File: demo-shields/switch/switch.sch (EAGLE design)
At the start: 18 parts, among them J4 J5MM, T1 2N2222

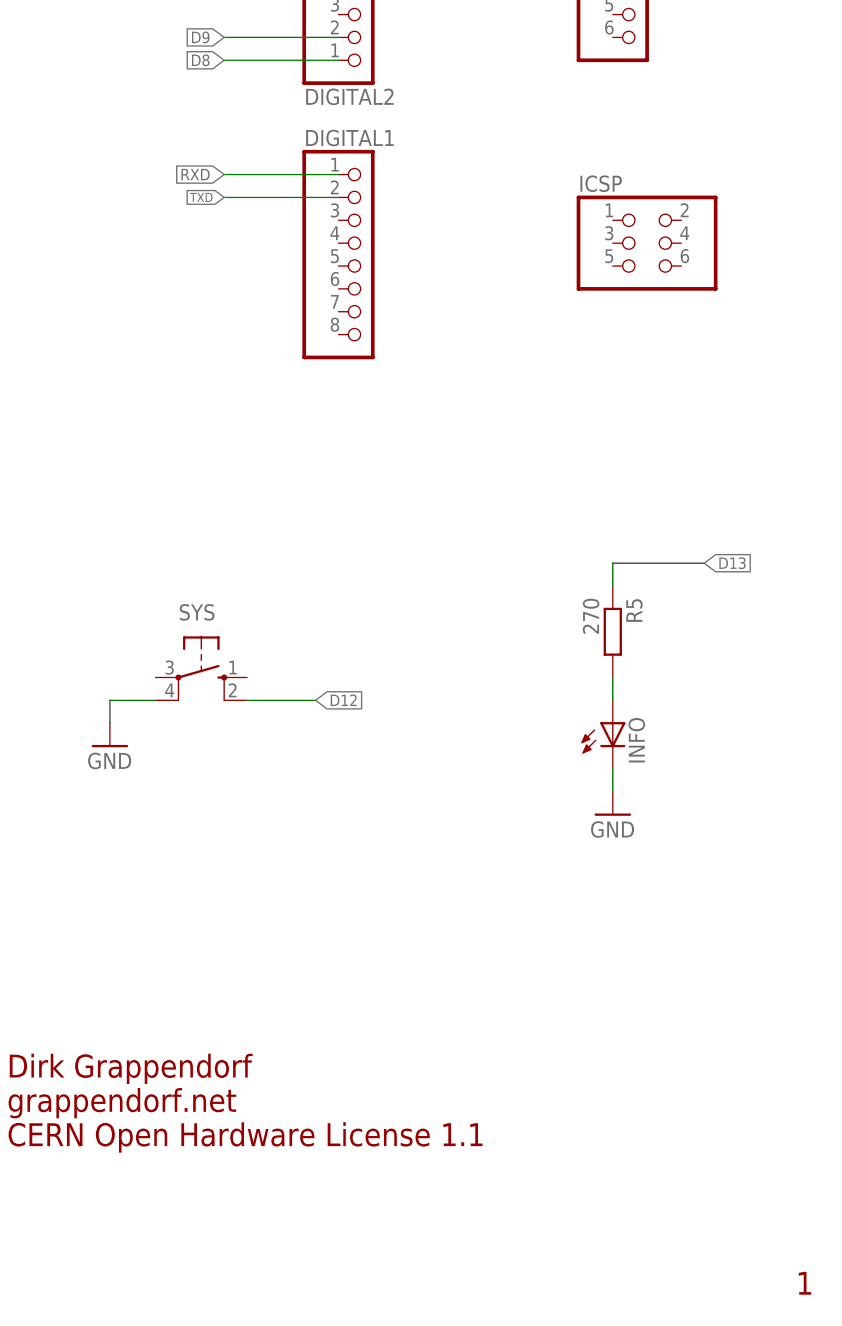
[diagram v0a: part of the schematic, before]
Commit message: fix: Use software serial for WiFly communication
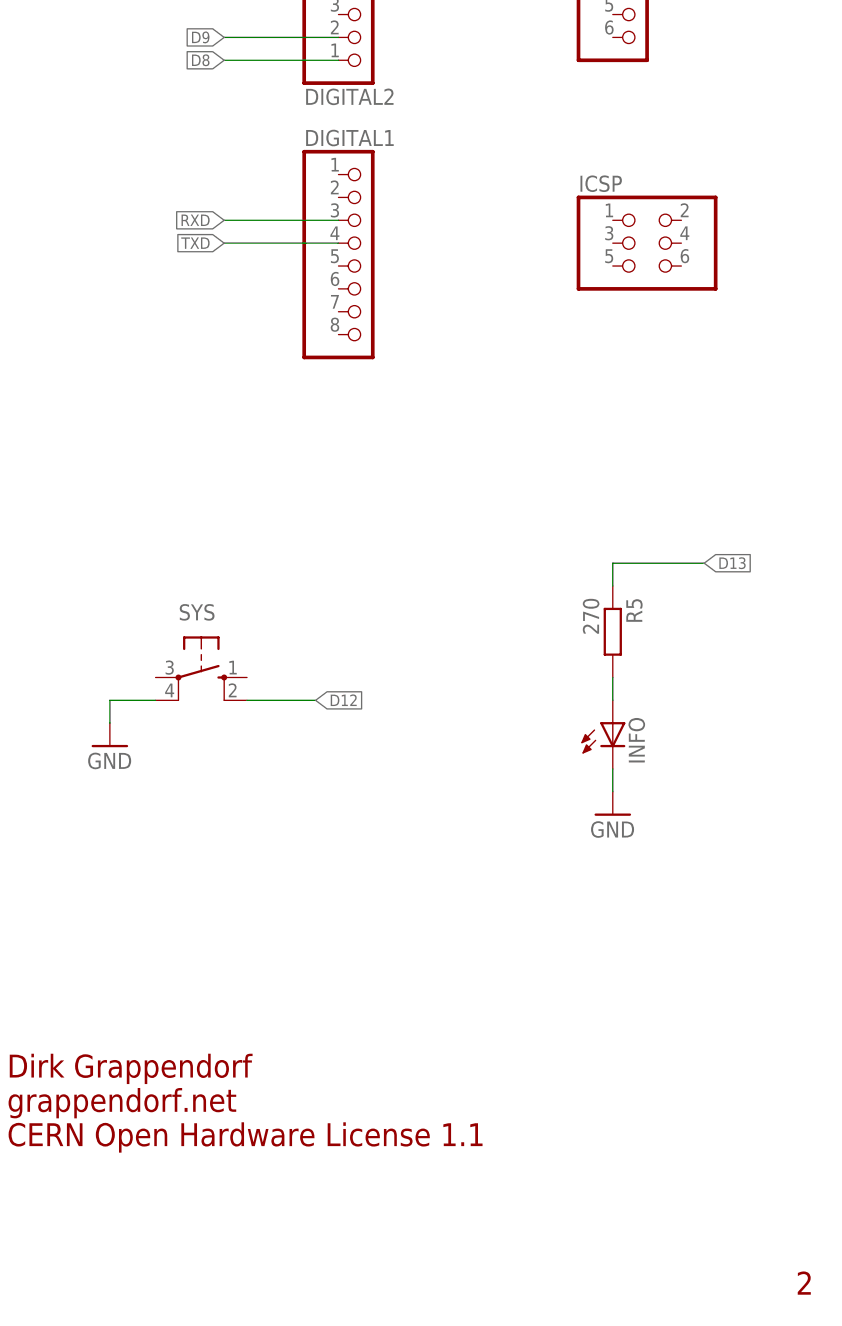
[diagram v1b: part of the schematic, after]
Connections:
- net RXD: now also DIGITAL1.3; no longer DIGITAL1.1
- net TXD: now also DIGITAL1.4; no longer DIGITAL1.2
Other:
- note added: "2"
- note removed: "1"
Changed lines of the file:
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@@
 <plain>
 <text x="163.83" y="31.75" size="2.54" layer="94">Dirk Grappendorf</text>
-<text x="251.46" y="7.62" size="2.54" layer="94">1</text>
+<text x="251.46" y="7.62" size="2.54" layer="94">2</text>
 <text x="163.83" y="27.94" size="2.54" layer="94">grappendorf.net</text>
 <text x="163.83" y="24.13" size="2.54" layer="94">CERN Open Hardware License 1.1</text>
@@
 <net name="RXD" class="0">
 <segment>
-<pinref part="DIGITAL1" gate="A" pin="1"/>
-<wire x1="200.66" y1="132.08" x2="187.96" y2="132.08" width="0.1524" layer="91"/>
-<label x="187.96" y="132.08" size="1.27" layer="95" rot="R180" xref="yes"/>
-</segment>
-<segment>
 <pinref part="WIFLY" gate="G$1" pin="DOUT"/>
 <wire x1="45.72" y1="149.86" x2="38.1" y2="149.86" width="0.1524" layer="91"/>
 <label x="38.1" y="149.86" size="1.27" layer="95" rot="R180" xref="yes"/>
+</segment>
+<segment>
+<pinref part="DIGITAL1" gate="A" pin="3"/>
+<wire x1="200.66" y1="127" x2="187.96" y2="127" width="0.1524" layer="91"/>
+<label x="187.96" y="127" size="1.27" layer="95" rot="R180" xref="yes"/>
 </segment>
 </net>
@@
 <net name="TXD" class="0">
 <segment>
-<pinref part="DIGITAL1" gate="A" pin="2"/>
-<wire x1="200.66" y1="129.54" x2="187.96" y2="129.54" width="0.1524" layer="91"/>
-<label x="187.96" y="129.54" size="1.016" layer="95" rot="R180" xref="yes"/>
-</segment>
-<segment>
 <pinref part="R1" gate="G$1" pin="2"/>
 <wire x1="25.4" y1="160.02" x2="25.4" y2="162.56" width="0.1524" layer="91"/>
@@
 <label x="17.78" y="162.56" size="1.27" layer="95" rot="R180" xref="yes"/>
 </segment>
+<segment>
+<pinref part="DIGITAL1" gate="A" pin="4"/>
+<wire x1="200.66" y1="124.46" x2="187.96" y2="124.46" width="0.1524" layer="91"/>
+<label x="187.96" y="124.46" size="1.27" layer="95" rot="R180" xref="yes"/>
+</segment>
 </net>
